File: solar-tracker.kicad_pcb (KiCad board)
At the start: 2 copper layers, 135.9 x 47 mm, 30 parts, among them J1 LDR1, J2 LDR2, J3 Motor, J4 Power_9V, J5 FWD_Limit, J6 REV_Limit, Q1 TIP41C, Q2 TIP41C, Q3 TIP42C, Q4 TIP42C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

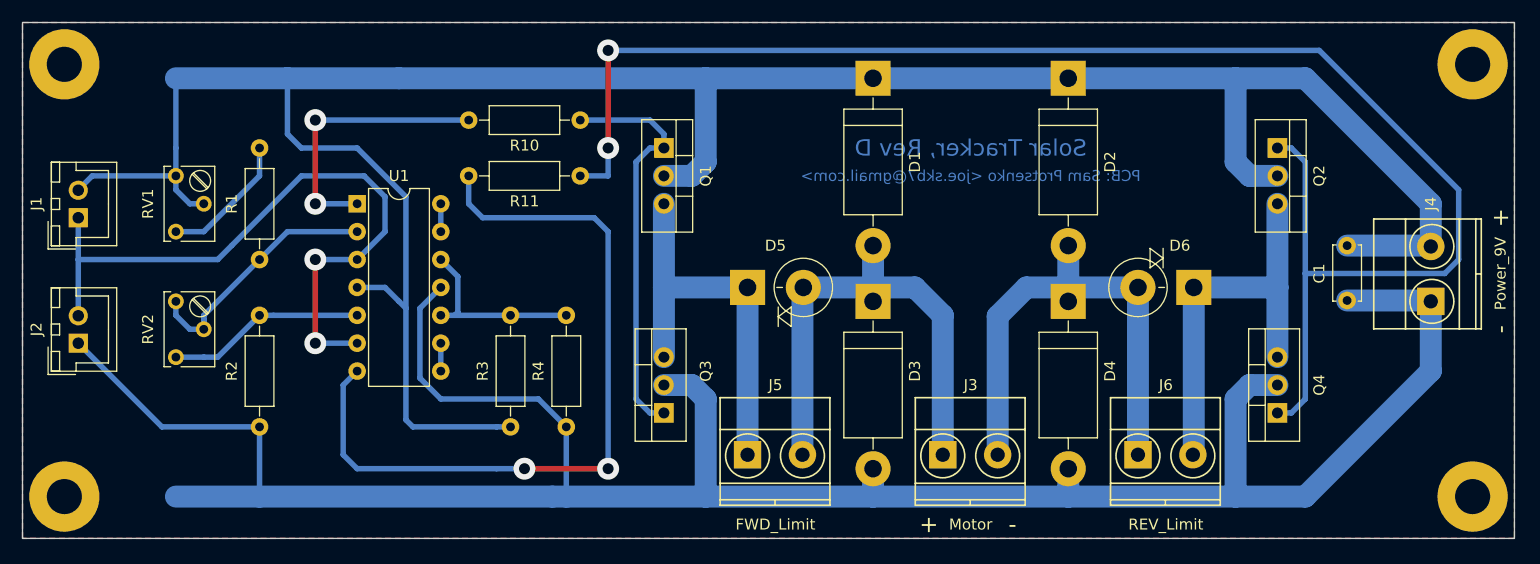
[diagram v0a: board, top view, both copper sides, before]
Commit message: Migrate to KiCad 5.0
Signed-off-by: Sam Protsenko <joe.skb7@gmail.com>
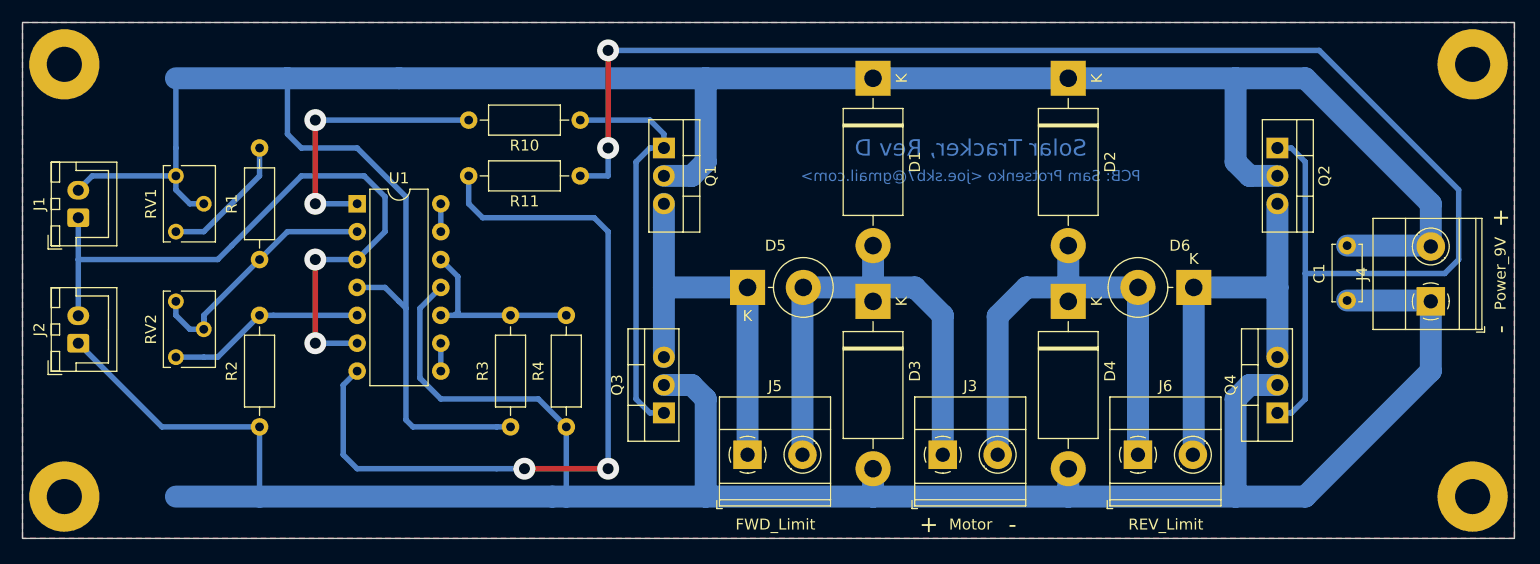
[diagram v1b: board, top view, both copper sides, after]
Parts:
- C1: footprint Capacitors_THT:C_Disc_D5.0mm_W2.5mm_P5.00mm -> Capacitor_THT:C_Disc_D5.0mm_W2.5mm_P5.00mm
- D1, D2, D3, D4: footprint Diodes_THT:D_DO-201AD_P15.24mm_Horizontal -> Diode_THT:D_DO-201AD_P15.24mm_Horizontal
- D5, D6: footprint Diodes_THT:D_DO-201AD_P5.08mm_Vertical_KathodeUp -> Diode_THT:D_DO-201AD_P5.08mm_Vertical_KathodeUp
- J1, J2: footprint Connectors_JST:JST_XH_B02B-XH-A_02x2.50mm_Straight -> Connector_JST:JST_XH_B02B-XH-A_1x02_P2.50mm_Vertical
- J3, J4, J5, J6: footprint Connectors_Terminal_Blocks:TerminalBlock_Pheonix_MKDS1.5-2pol -> TerminalBlock_Phoenix:TerminalBlock_Phoenix_MKDS-1,5-2_1x02_P5.00mm_Horizontal
- MK1, MK2, MK3, MK4: footprint Mounting_Holes:MountingHole_3.2mm_M3_Pad -> MountingHole:MountingHole_3.2mm_M3_Pad
- Q1, Q2, Q3, Q4: footprint TO_SOT_Packages_THT:TO-220_Vertical -> Package_TO_SOT_THT:TO-220-3_Vertical
- R1, R10, R11, R2, R3, R4: footprint Resistors_THT:R_Axial_DIN0207_L6.3mm_D2.5mm_P10.16mm_Horizontal -> Resistor_THT:R_Axial_DIN0207_L6.3mm_D2.5mm_P10.16mm_Horizontal
- RV1, RV2: footprint Potentiometers:Potentiometer_Trimmer_Bourns_3266W -> Potentiometer_THT:Potentiometer_Bourns_3266W_Vertical
- U1: footprint Housings_DIP:DIP-14_W7.62mm -> Package_DIP:DIP-14_W7.62mm
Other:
- board text added: "FWD_Limit"
- board text added: "Motor"
- board text added: "Power_9V"
- board text added: "REV_Limit"
